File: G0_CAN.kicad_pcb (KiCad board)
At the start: 2 copper layers, 69.8 x 53.3 mm, 31 parts, among them J1 USB_C_Receptacle_USB2.0, J2 CAN1, J3 CAN2, U1 Nucleo-64-G0B1, U2 TJA1051TK-3, U3 TJA1051TK-3

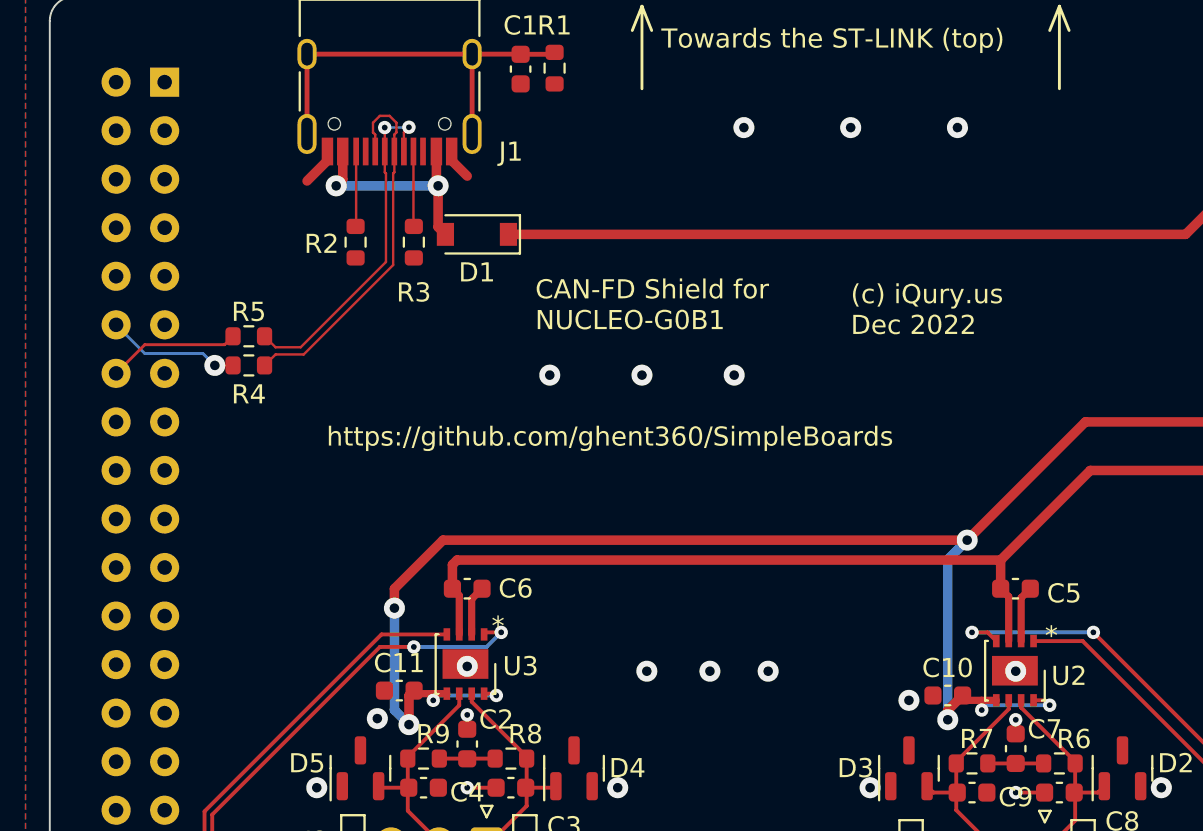
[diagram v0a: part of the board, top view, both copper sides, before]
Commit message: Fix S pin on the CAN transcievers to low, so they are active. Fix USB data pin routing.
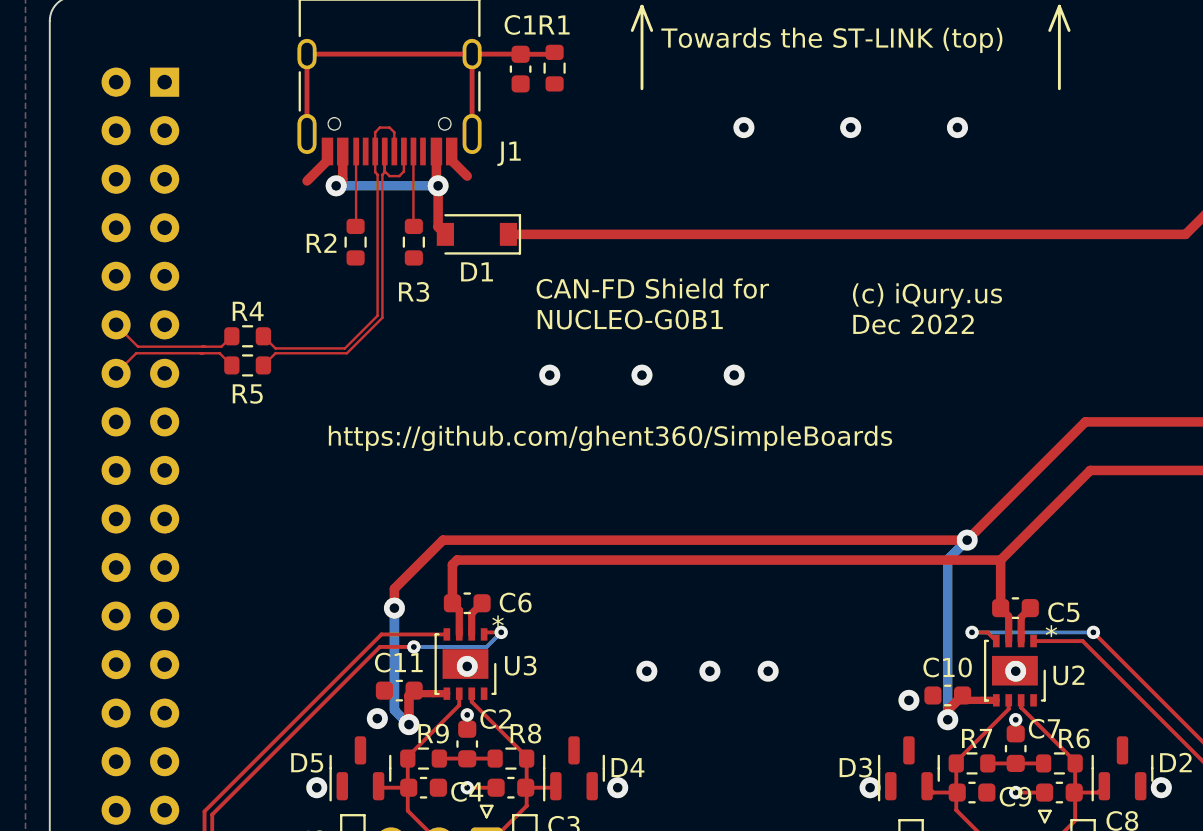
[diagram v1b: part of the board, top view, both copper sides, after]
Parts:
- moved R4 1.53 mm to (62.4, 81.3)
- moved R5 1.53 mm to (62.4, 82.8)
- moved C5 1.02 mm to (102.6, 95.5)
- moved C6 0.76 mm to (73.9, 95.2)
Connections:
- U2 pad 8: /3.3V -> GND
- U3 pad 8: /3.3V -> GND
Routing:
- net /3.3V: track 83.9 -> 74.4 mm, vias 8 -> 4
- net GND: track 13.7 -> 11.9 mm
- net /D-: track 18.2 -> 19.3 mm, vias 2 -> 0
- net /D+: track 19.5 -> 18.8 mm
- net /USB_DP: track 7.00 -> 6.92 mm, vias 1 -> 0

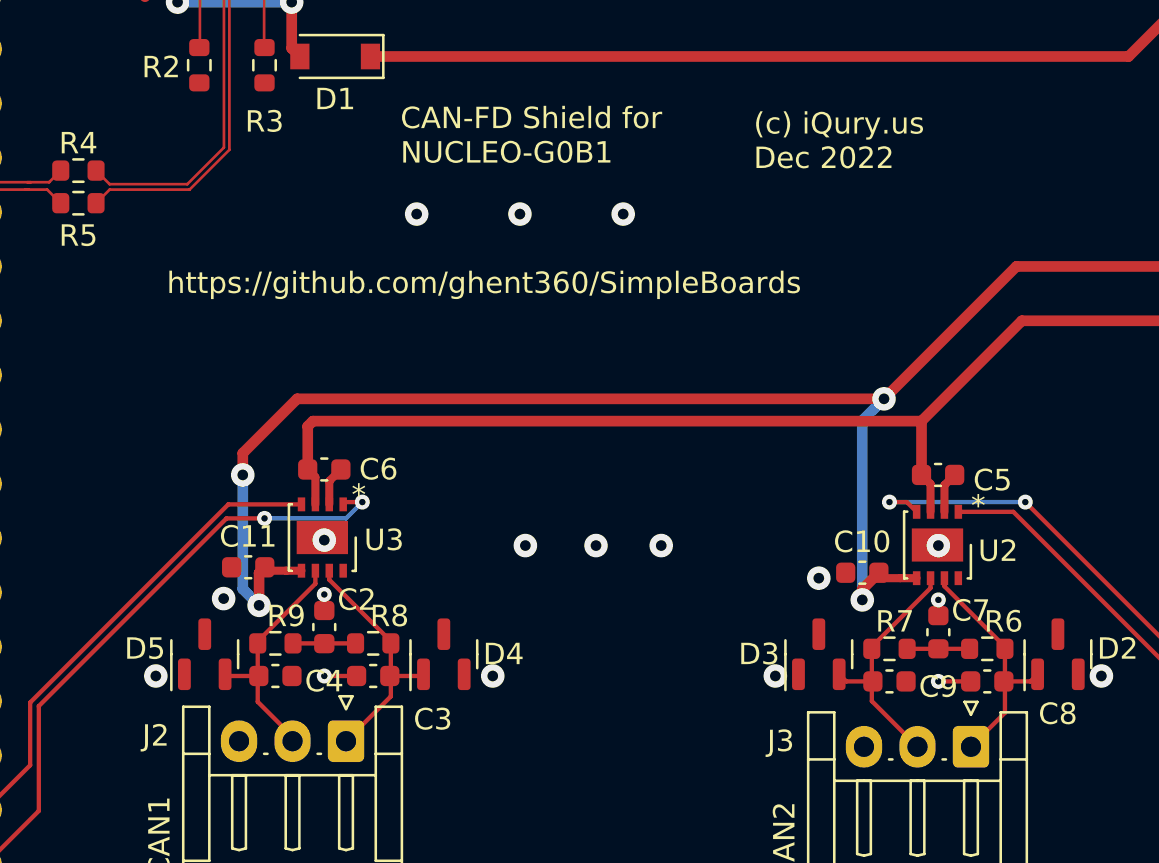
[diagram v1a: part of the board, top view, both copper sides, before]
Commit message: Update the CAN filter network routing.
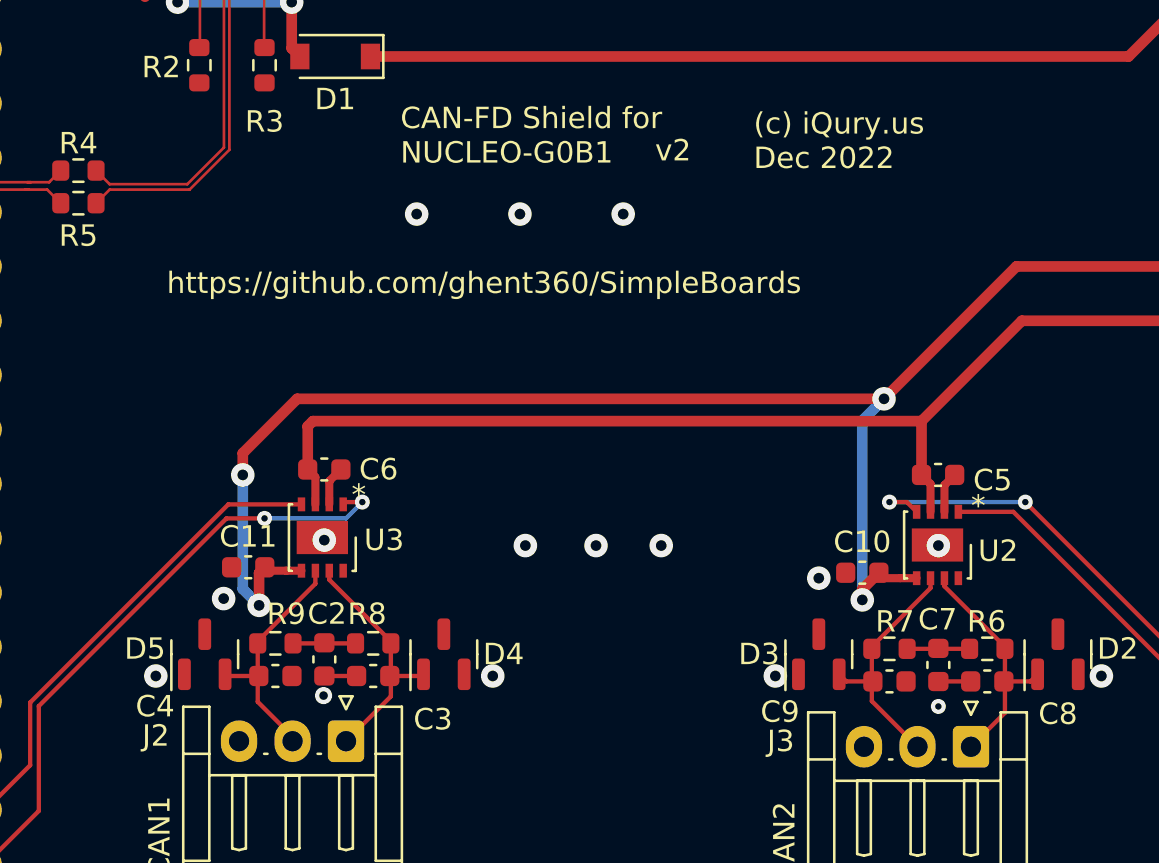
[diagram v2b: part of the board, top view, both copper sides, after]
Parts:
- moved C7 1.53 mm to (102.6, 104.4), turned to -90 degrees
- moved C2 1.51 mm to (73.9, 104.1), turned to -90 degrees
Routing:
- net GND: track 11.9 -> 10.4 mm, vias 21 -> 19
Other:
- board text added: "v2"
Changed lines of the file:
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@@
     (property "ki_keywords" "R res resistor")
     (attr smd)
-    (fp_text reference "R6" (at -0.762 1.27) (layer "F.SilkS")
+    (fp_text reference "R6" (at 0.034026 1.27) (layer "F.SilkS")
         (effects (font (size 1 1) (thickness 0.15)))
     )
@@
   )
   (footprint "Capacitor_SMD:C_0603_1608Metric" (layer "F.Cu")
-    (at 102.616 102.857 90)
+    (at 102.615102 104.386452 -90)
     (descr "Capacitor SMD 0603 (1608 Metric), square (rectangular) end terminal, IPC_7351 nominal, (Body size source: IPC-SM-782 page 76, https://www.pcb-3d.com/wordpress/wp-content/uploads/ipc-sm-782a_amendment_1_and_2.pdf), generated with kicad-footprint-generator")
     (tags "capacitor")
@@
     (property "ki_keywords" "cap capacitor")
     (attr smd)
-    (fp_text reference "C7" (at 1.003 1.524 180) (layer "F.SilkS")
+    (fp_text reference "C7" (at -2.124452 0.033128) (layer "F.SilkS")
         (effects (font (size 1 1) (thickness 0.15)))
     )
@@
     (fp_line (start 0.8 0.4) (end -0.8 0.4)
       (stroke (width 0.1) (type solid)) (layer "F.Fab"))
-    (pad "1" smd roundrect (at -0.775 0 90) (size 0.9 0.95) (layers "F.Cu" "F.Paste" "F.Mask") (roundrect_rratio 0.25)
+    (pad "1" smd roundrect (at -0.775 0 270) (size 0.9 0.95) (layers "F.Cu" "F.Paste" "F.Mask") (roundrect_rratio 0.25)
       (net 7 "Net-(C7-Pad1)") (pintype "passive"))
-    (pad "2" smd roundrect (at 0.775 0 90) (size 0.9 0.95) (layers "F.Cu" "F.Paste" "F.Mask") (roundrect_rratio 0.25)
+    (pad "2" smd roundrect (at 0.775 0 270) (size 0.9 0.95) (layers "F.Cu" "F.Paste" "F.Mask") (roundrect_rratio 0.25)
       (net 2 "GND") (pintype "passive"))
     (model "${KICAD6_3DMODEL_DIR}/Capacitor_SMD.3dshapes/C_0603_1608Metric.wrl"
@@
   )
   (footprint "Capacitor_SMD:C_0603_1608Metric" (layer "F.Cu")
-    (at 73.914 102.616 90)
+    (at 73.91594 104.125952 -90)
     (descr "Capacitor SMD 0603 (1608 Metric), square (rectangular) end terminal, IPC_7351 nominal, (Body size source: IPC-SM-782 page 76, https://www.pcb-3d.com/wordpress/wp-content/uploads/ipc-sm-782a_amendment_1_and_2.pdf), generated with kicad-footprint-generator")
     (tags "capacitor")
@@
     (property "ki_keywords" "cap capacitor")
     (attr smd)
-    (fp_text reference "C2" (at 1.27 1.524 180) (layer "F.SilkS")
+    (fp_text reference "C2" (at -2.127703 -0.127813) (layer "F.SilkS")
         (effects (font (size 1 1) (thickness 0.15)))
     )
@@
     (fp_line (start 0.8 0.4) (end -0.8 0.4)
       (stroke (width 0.1) (type solid)) (layer "F.Fab"))
-    (pad "1" smd roundrect (at -0.775 0 90) (size 0.9 0.95) (layers "F.Cu" "F.Paste" "F.Mask") (roundrect_rratio 0.25)
+    (pad "1" smd roundrect (at -0.775 0 270) (size 0.9 0.95) (layers "F.Cu" "F.Paste" "F.Mask") (roundrect_rratio 0.25)
       (net 3 "Net-(C2-Pad1)") (pintype "passive"))
-    (pad "2" smd roundrect (at 0.775 0 90) (size 0.9 0.95) (layers "F.Cu" "F.Paste" "F.Mask") (roundrect_rratio 0.25)
+    (pad "2" smd roundrect (at 0.775 0 270) (size 0.9 0.95) (layers "F.Cu" "F.Paste" "F.Mask") (roundrect_rratio 0.25)
       (net 2 "GND") (pintype "passive"))
     (model "${KICAD6_3DMODEL_DIR}/Capacitor_SMD.3dshapes/C_0603_1608Metric.wrl"
@@
     (property "ki_keywords" "R res resistor")
     (attr smd)
-    (fp_text reference "R8" (at -0.762 1.27) (layer "F.SilkS")
+    (fp_text reference "R8" (at 0.288026 1.37) (layer "F.SilkS")
         (effects (font (size 1 1) (thickness 0.15)))
     )
@@
     (property "ki_keywords" "cap capacitor")
     (attr smd)
-    (fp_text reference "C9" (at -2.286 -0.254) (layer "F.SilkS")
+    (fp_text reference "C9" (at 5.114026 -1.424) (layer "F.SilkS")
         (effects (font (size 1 1) (thickness 0.15)))
     )
@@
     (property "ki_keywords" "R res resistor")
     (attr smd)
-    (fp_text reference "R9" (at -0.508 1.27) (layer "F.SilkS")
+    (fp_text reference "R9" (at -0.508 1.37) (layer "F.SilkS")
         (effects (font (size 1 1) (thickness 0.15)))
     )
@@
     (property "ki_keywords" "cap capacitor")
     (attr smd)
-    (fp_text reference "C4" (at -2.286 -0.254) (layer "F.SilkS")
+    (fp_text reference "C4" (at 5.622026 -1.424) (layer "F.SilkS")
         (effects (font (size 1 1) (thickness 0.15)))
     )
@@
     (effects (font (size 1 1) (thickness 0.15)) (justify left bottom))
   )
+  (gr_text "v2" (at 89.373974 80.926) (layer "F.SilkS")
+    (effects (font (size 1 1) (thickness 0.15)) (justify left bottom))
+  )
   (gr_text "*" (at 75.184 97.028) (layer "F.SilkS")
     (effects (font (size 1 1) (thickness 0.15)) (justify left bottom))
@@
   (segment (start 74.17 66.514) (end 76.7 66.514) (width 0.254) (layer "F.Cu") (net 1))
   (segment (start 66.6 71.609) (end 66.6 72.084) (width 0.5) (layer "F.Cu") (net 2))
-  (segment (start 73.914 101.841) (end 73.914 101.092) (width 0.2032) (layer "F.Cu") (net 2))
   (segment (start 73.1 71.609) (end 73.1 72.084) (width 0.5) (layer "F.Cu") (net 2))
   (segment (start 66.6 72.084) (end 65.532 73.152) (width 0.5) (layer "F.Cu") (net 2))
-  (segment (start 102.616 102.082) (end 102.616 101.346) (width 0.2032) (layer "F.Cu") (net 2))
   (segment (start 102.9 95.982) (end 103.378 95.504) (width 0.381) (layer "F.Cu") (net 2))
   (segment (start 75.425 104.902) (end 73.914 104.902) (width 0.2032) (layer "F.Cu") (net 2))
@@
   (segment (start 73.1 72.084) (end 73.914 72.898) (width 0.5) (layer "F.Cu") (net 2))
   (via (at 81.788 104.902) (size 1.1) (drill 0.5) (layers "F.Cu" "B.Cu") (free) (net 2))
-  (via (at 73.914 101.092) (size 0.7) (drill 0.3) (layers "F.Cu" "B.Cu") (net 2))
   (via (at 88.392 70.358) (size 1.1) (drill 0.5) (layers "F.Cu" "B.Cu") (free) (net 2))
   (via (at 78.232 83.312) (size 1.1) (drill 0.5) (layers "F.Cu" "B.Cu") (free) (net 2))
@@
   (via (at 99.568 70.358) (size 1.1) (drill 0.5) (layers "F.Cu" "B.Cu") (free) (net 2))
   (via (at 94.996 104.902) (size 1.1) (drill 0.5) (layers "F.Cu" "B.Cu") (free) (net 2))
-  (via (at 102.616 101.346) (size 0.7) (drill 0.3) (layers "F.Cu" "B.Cu") (net 2))
   (via (at 89.662 98.806) (size 1.1) (drill 0.5) (layers "F.Cu" "B.Cu") (free) (net 2))
   (via (at 97.028 100.33) (size 1.1) (drill 0.5) (layers "F.Cu" "B.Cu") (free) (net 2))
   (via (at 83.312 98.806) (size 1.1) (drill 0.5) (layers "F.Cu" "B.Cu") (free) (net 2))
-  (via (at 73.914 104.902) (size 0.7) (drill 0.3) (layers "F.Cu" "B.Cu") (net 2))
   (via (at 110.236 104.902) (size 1.1) (drill 0.5) (layers "F.Cu" "B.Cu") (free) (net 2))
   (via (at 69.21002 101.28499) (size 1.1) (drill 0.5) (layers "F.Cu" "B.Cu") (free) (net 2))
@@
   (via (at 93.98 70.358) (size 1.1) (drill 0.5) (layers "F.Cu" "B.Cu") (free) (net 2))
   (via (at 86.614 98.806) (size 1.1) (drill 0.5) (layers "F.Cu" "B.Cu") (free) (net 2))
-  (via (at 102.616 105.156) (size 0.7) (drill 0.3) (layers "F.Cu" "B.Cu") (net 2))
+  (via (at 102.616 106.326) (size 0.7) (drill 0.3) (layers "F.Cu" "B.Cu") (net 2))
+  (via (at 73.879974 105.818) (size 0.8) (drill 0.4) (layers "F.Cu" "B.Cu") (free) (net 2))
   (via (at 73.914 98.552) (size 1.1) (drill 0.5) (layers "F.Cu" "B.Cu") (net 2))
   (via (at 102.616 98.806) (size 1.1) (drill 0.5) (layers "F.Cu" "B.Cu") (net 2))
